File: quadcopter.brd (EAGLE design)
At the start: 143.4 x 143.4 mm, 69 parts, among them J1 AVR_SPI_PRG_6NS, U1 ATMEGA128RFA1, Y2 16MHz

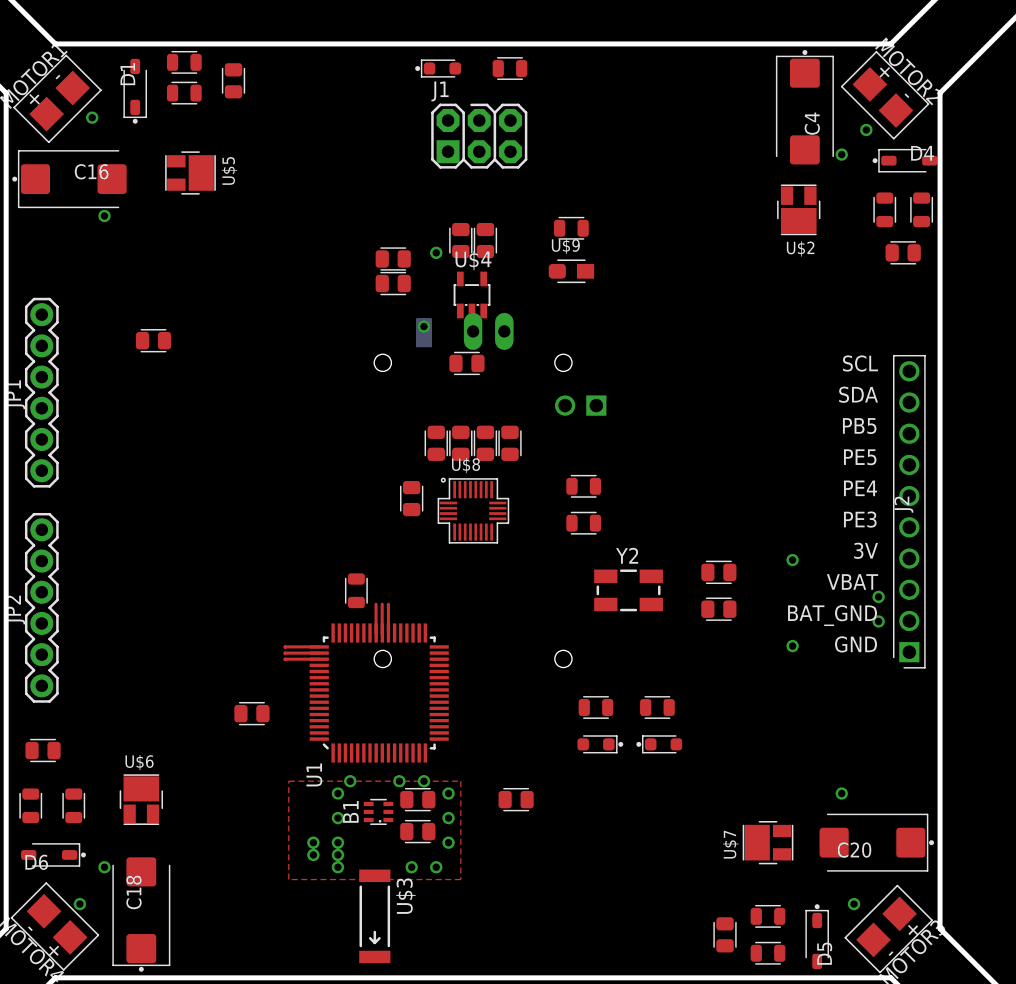
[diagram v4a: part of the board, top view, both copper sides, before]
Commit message: Optimized clock and antenna placement, fixed net bridge, misc. optimizations.
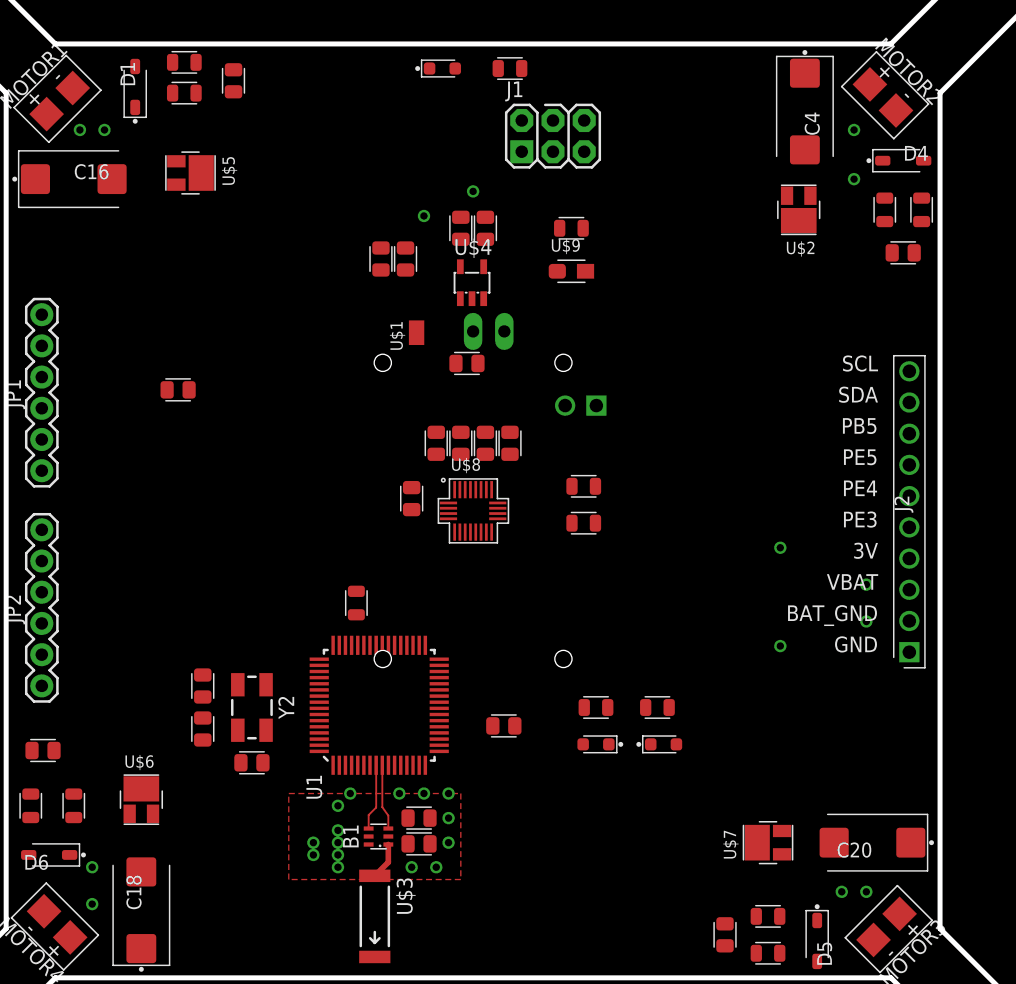
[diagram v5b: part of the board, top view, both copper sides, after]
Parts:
- moved C5 43.9 mm to (16.0, 20.2), turned to 270 degrees
- moved C6 42.5 mm to (16.0, 23.8), turned to 90 degrees
- moved Y2 32.1 mm to (20.0, 22.0), turned to 270 degrees
- moved C7 6.08 mm to (40.5, 20.5), turned to 0 degrees
- moved J1 6.00 mm to (44.5, 68.5)
- moved C13 4.47 mm to (14.0, 47.9)
- moved C8 4.00 mm to (20.0, 17.5), turned to 180 degrees
- moved C11 2.24 mm to (30.5, 58.5), turned to 270 degrees
- moved B1 2.00 mm to (30.3, 11.5)
- moved C9 1.50 mm to (33.6, 13.0)
- moved C10 1.00 mm to (33.6, 10.9)
- moved C12 1.00 mm to (32.5, 58.5), turned to 270 degrees
- moved C14 1.00 mm to (39.0, 61.0)
- moved C3 1.00 mm to (37.0, 61.0)
- moved R5 1.00 mm to (28.5, 30.5)
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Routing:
- net N$9: track 0.00 -> 5.40 mm
- net N$10: track 0.00 -> 5.31 mm
- net N$12: track 0.00 -> 3.00 mm
- net PE5: track 2.81 -> 0.00 mm
- net PE4: track 2.81 -> 0.00 mm
- net PE3: track 2.81 -> 0.00 mm
- net PB5: track 2.35 -> 0.00 mm
- net PB4: track 2.35 -> 0.00 mm
- net MISO: track 2.34 -> 0.00 mm

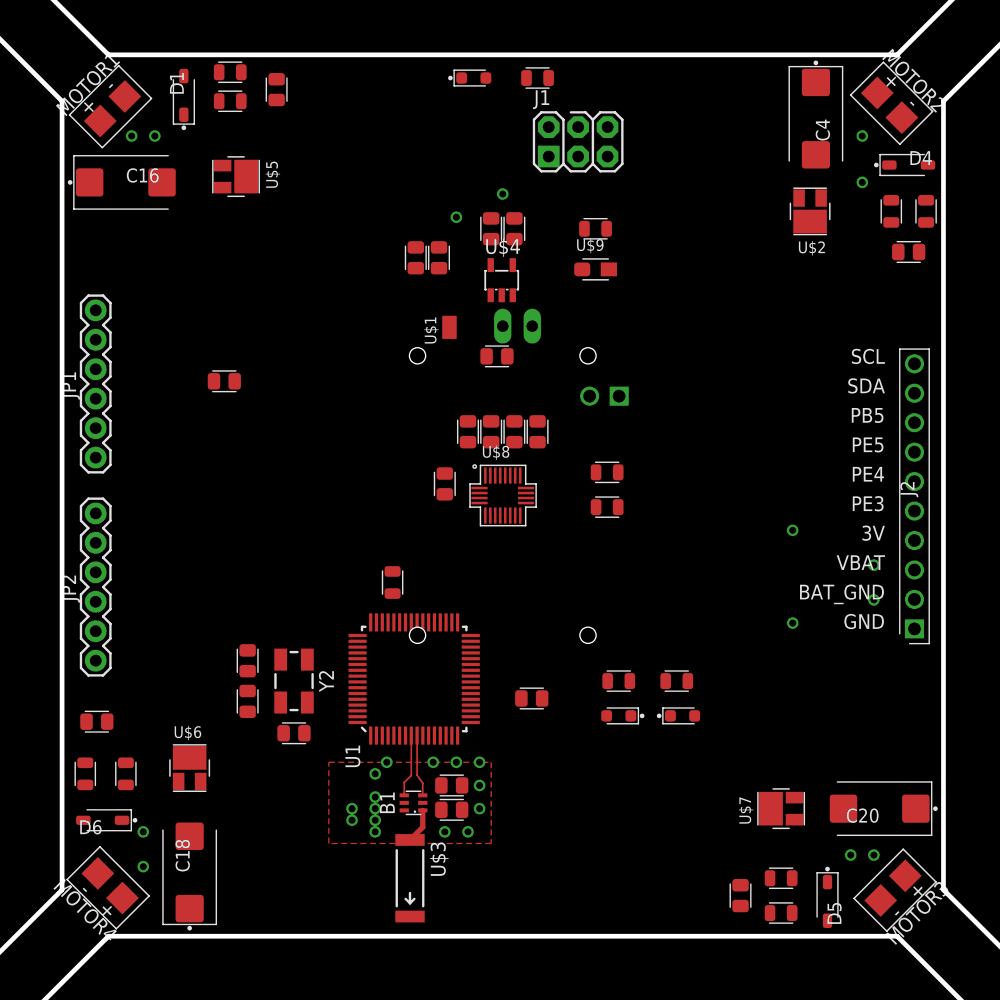
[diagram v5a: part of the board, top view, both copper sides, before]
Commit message: Board fully routed
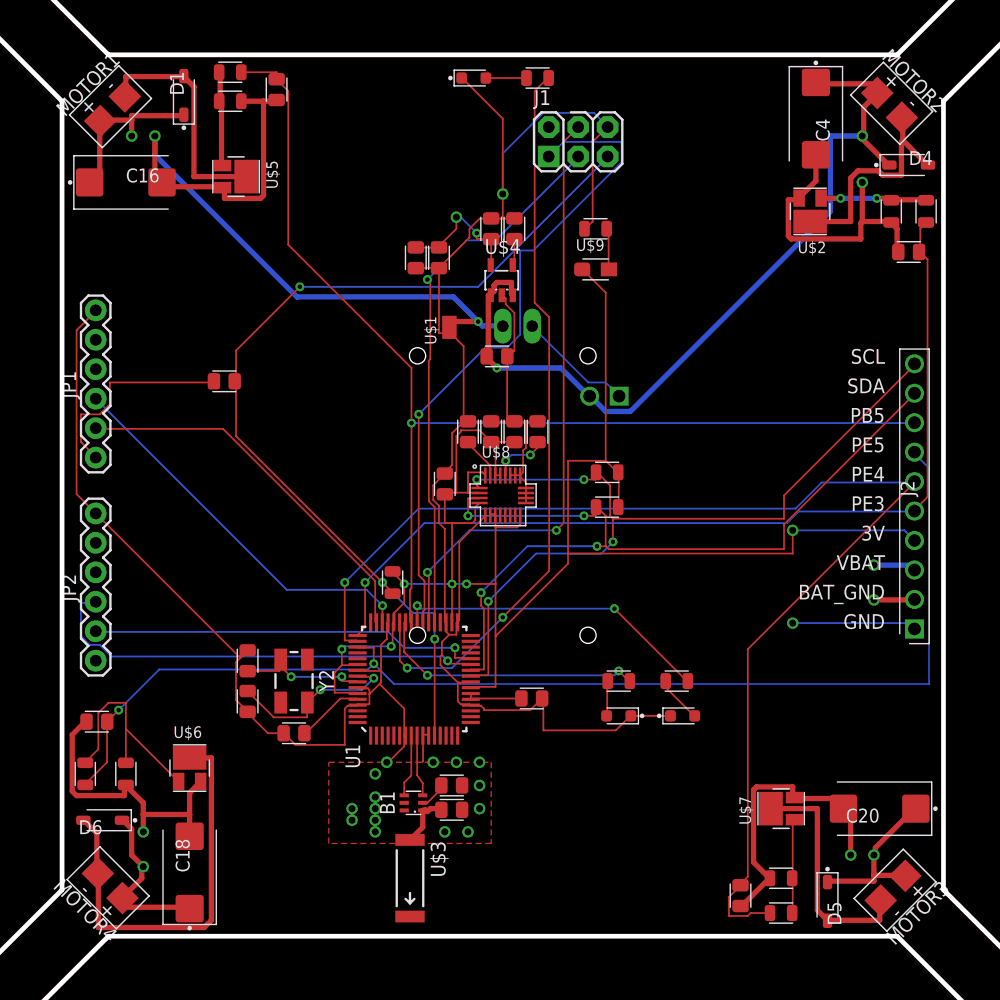
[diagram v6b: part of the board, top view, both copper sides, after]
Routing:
- net GND: track 0.00 -> 244.0 mm
- net 3V: track 0.00 -> 170.5 mm, vias 2 -> 8
- net BAT_GND: track 0.00 -> 146.2 mm, vias 5 -> 6
- net VBAT: track 0.00 -> 119.2 mm, vias 5 -> 6
- net PE4: track 0.00 -> 106.6 mm, vias 0 -> 1
- net PE5: track 0.00 -> 103.3 mm, vias 0 -> 2
- net PB5: track 0.00 -> 98.8 mm, vias 0 -> 1
- net RESET: track 0.00 -> 81.9 mm, vias 0 -> 3
- net PE3: track 0.00 -> 80.7 mm, vias 0 -> 1
- net SCL: track 0.00 -> 72.0 mm, vias 0 -> 4
- net SDA: track 0.00 -> 72.0 mm, vias 0 -> 4
- net PB7: track 0.00 -> 63.5 mm, vias 0 -> 2
- net MISO: track 0.00 -> 57.5 mm, vias 0 -> 1
- net MOSI: track 0.00 -> 52.5 mm, vias 0 -> 2
- net SCK: track 0.00 -> 47.4 mm, vias 0 -> 1
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
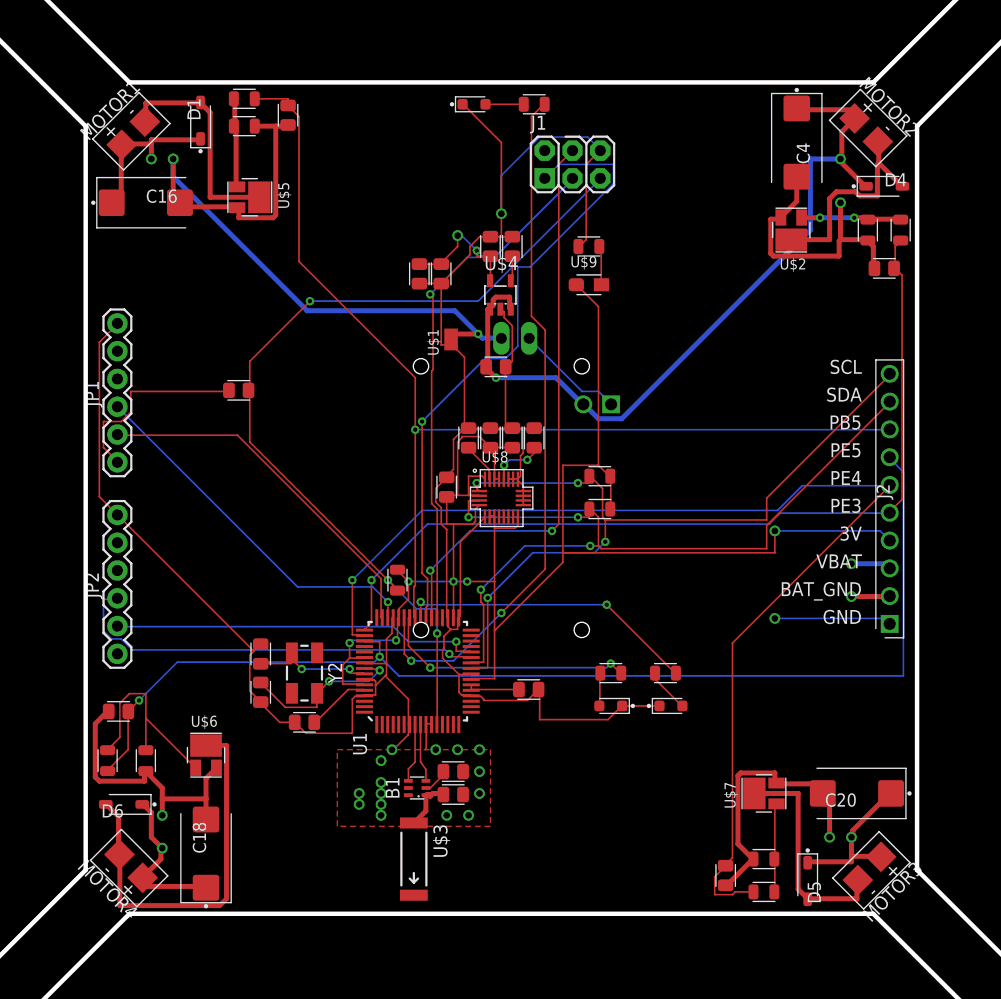
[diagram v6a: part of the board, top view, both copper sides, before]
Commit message: Removed filter/flyback labels in schematic, refined placement of many board components
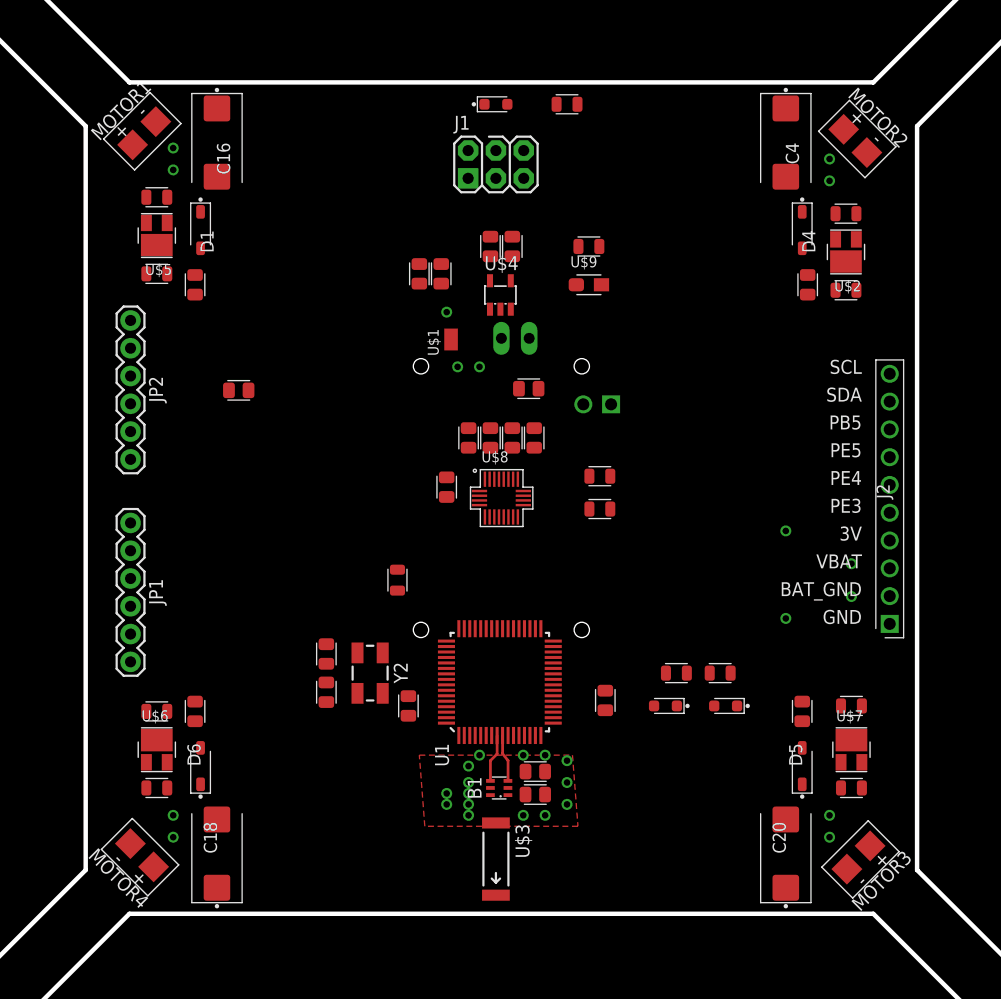
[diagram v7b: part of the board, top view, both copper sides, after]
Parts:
- moved JP2 30.5 mm to (4.10, 54.2), turned to 270 degrees
- moved R10 18.8 mm to (70.0, 19.0), turned to 180 degrees
- moved R6 17.9 mm to (6.50, 58.5), turned to 0 degrees
- moved C15 17.7 mm to (10.0, 57.5), turned to 90 degrees
- moved C19 16.6 mm to (65.5, 18.5)
- moved D5 10.5 mm to (65.5, 13.5), turned to 90 degrees
- moved R11 10.3 mm to (70.0, 11.5), turned to 180 degrees
- moved R7 10.3 mm to (6.50, 65.5), turned to 0 degrees
- moved D1 10.0 mm to (10.5, 62.5), turned to 270 degrees
- moved C8 9.62 mm to (29.5, 19.0), turned to 270 degrees
- moved U$5 9.19 mm to (6.50, 62.0), turned to 180 degrees
- moved U$7 8.94 mm to (70.0, 15.0), turned to 0 degrees
- moved C16 8.51 mm to (12.0, 70.5), turned to 270 degrees
- moved C20 8.51 mm to (64.0, 5.50), turned to 90 degrees
- moved D4 8.50 mm to (65.5, 62.5), turned to 270 degrees
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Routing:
- net GND: track 244.0 -> 0.00 mm
- net 3V: track 170.5 -> 0.00 mm, vias 8 -> 1
- net BAT_GND: track 146.2 -> 0.00 mm
- net VBAT: track 119.2 -> 0.00 mm
- net PE4: track 106.6 -> 0.00 mm, vias 1 -> 0
- net PE5: track 103.3 -> 0.00 mm, vias 2 -> 0
- net PB5: track 98.8 -> 0.00 mm, vias 1 -> 0
- net RESET: track 81.9 -> 0.00 mm, vias 3 -> 0
- net PE3: track 80.7 -> 0.00 mm, vias 1 -> 0
- net SCL: track 72.0 -> 0.00 mm, vias 4 -> 0
- net SDA: track 72.0 -> 0.00 mm, vias 4 -> 0
- net PB7: track 63.5 -> 0.00 mm, vias 2 -> 0
- net MISO: track 57.5 -> 0.00 mm, vias 1 -> 0
- net MOSI: track 52.5 -> 0.00 mm, vias 2 -> 0
- net SCK: track 47.4 -> 0.00 mm, vias 1 -> 0
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- added copper zone on layer 15, net N$15
